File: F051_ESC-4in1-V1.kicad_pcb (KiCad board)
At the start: 4 copper layers, 46 x 55.8 mm, 222 parts, among them J1 Conn_01x02, J11 Conn_01x03, J14 Conn_01x03, J2 Conn_01x10, J3 Conn_01x05, J4 Conn_01x05, J5 Conn_01x05, J6 Conn_01x03, J7 Conn_01x05, J8 Conn_01x03, J9 Conn_01x10, Q1 TPHR8504PL, Q10 TPHR8504PL, Q11 TPHR8504PL, Q12 TPHR8504PL, Q13 TPHR8504PL, Q14 TPHR8504PL, Q15 TPHR8504PL, Q16 TPHR8504PL, Q17 TPHR8504PL, Q18 TPHR8504PL, Q19 TPHR8504PL, Q2 TPHR8504PL, Q20 TPHR8504PL, Q21 TPHR8504PL, Q22 TPHR8504PL, Q23 TPHR8504PL, Q24 TPHR8504PL, Q3 TPHR8504PL, Q4 TPHR8504PL, Q5 TPHR8504PL, Q6 TPHR8504PL, Q7 TPHR8504PL, Q8 TPHR8504PL, Q9 TPHR8504PL, U1 STM32F051K6Ux, U10 FD6288Q, U11 STM32F051K6Ux, U12 FD6288Q, U13 L78L12_SOT89, U14 MP4560_QFN10, U2 FD6288Q, U3 L78L12_SOT89, U4 LP2985-3.3, U5 INA139, U6 FD6288Q, U7 OPA340NA, U8 STM32F051K6Ux, U9 STM32F051K6Ux

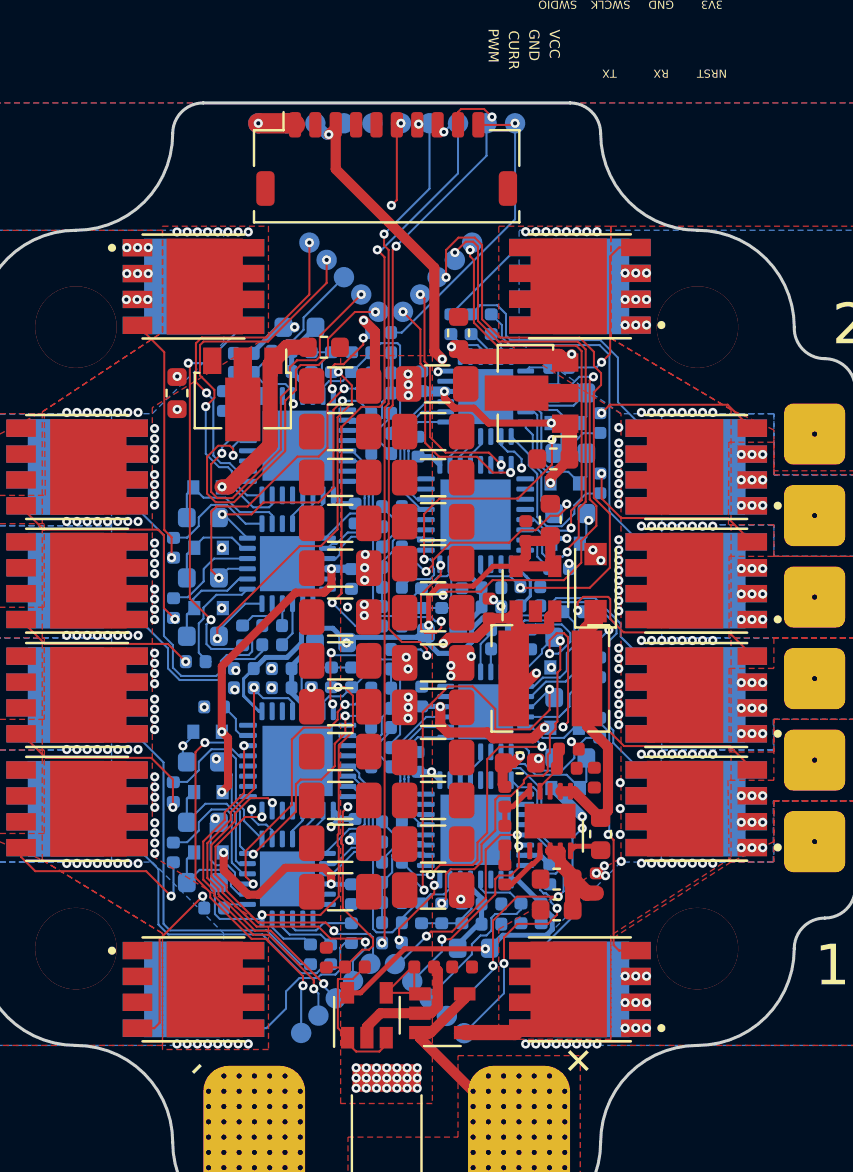
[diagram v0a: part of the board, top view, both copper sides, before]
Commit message: More GND and VCC vias and planes added.  Moved around some sense resistors to expose GND
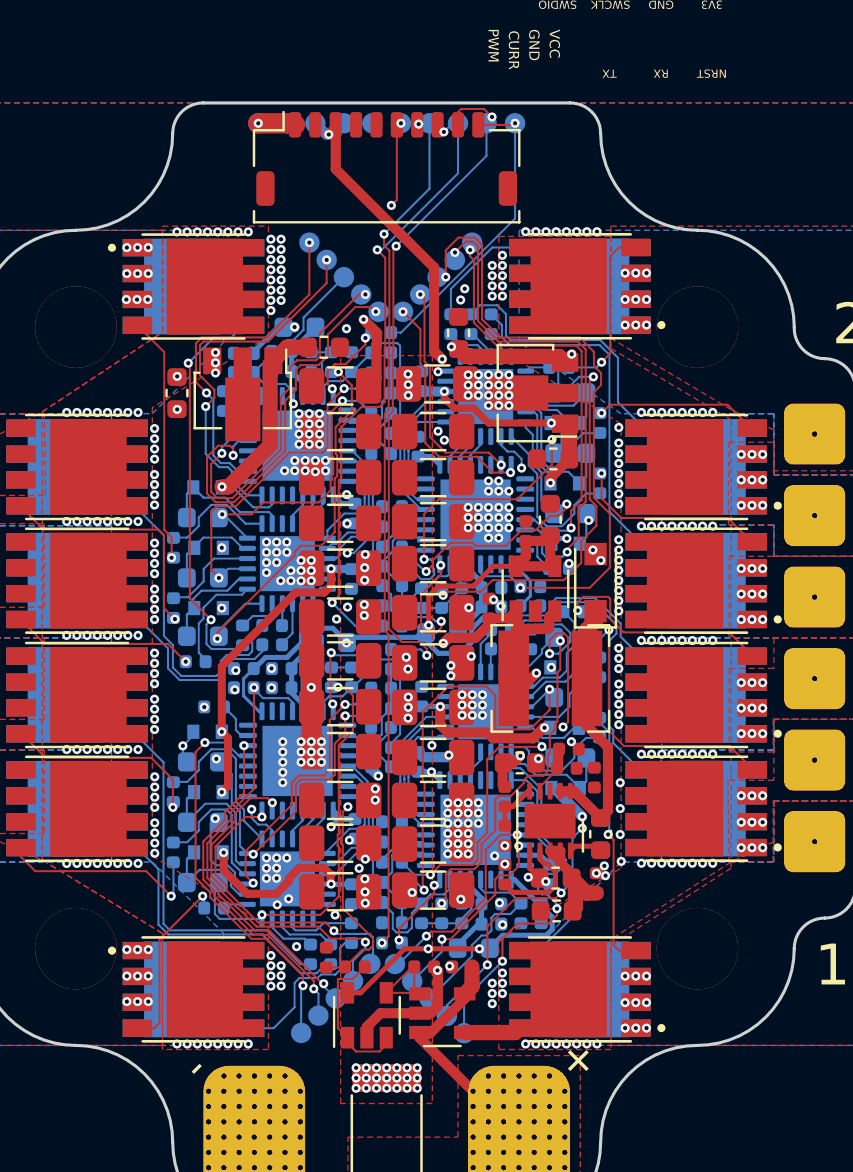
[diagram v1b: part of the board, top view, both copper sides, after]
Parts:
- moved R35 1.90 mm to (140.3, 86.9), turned to 0 degrees
- moved R29 1.04 mm to (140.3, 85.0)
- moved R30 1.02 mm to (140.3, 85.9), turned to 180 degrees
- moved R10 0.99 mm to (140.3, 101.5), turned to 180 degrees
- moved R15 0.99 mm to (140.3, 102.5), turned to 0 degrees
- moved C73 0.07 mm to (148.3, 100.3)
- moved C72 0.05 mm to (148.3, 101.9)
- turned R14 to 0 degrees
- turned R34 to 0 degrees
- turned R36 to 90 degrees
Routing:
- net GND: track 8.15 -> 21.9 mm, vias 141 -> 329
- net +3V3: track 70.6 -> 82.1 mm, vias 7 -> 12
- net Net-(R76-Pad1): track 2.59 -> 4.89 mm
- net VCC: track 7.09 -> 8.55 mm
- net VCC_Shunt: track 21.6 -> 20.2 mm, vias 151 -> 163
- net /MCU 2/SenseC: track 4.67 -> 3.73 mm
- net Net-(Q12-Pad4): track 4.94 -> 5.67 mm
- net /MCU 2/SenseB: track 5.18 -> 5.69 mm
- net /MCU 3/PhaseC: vias 2 -> 11

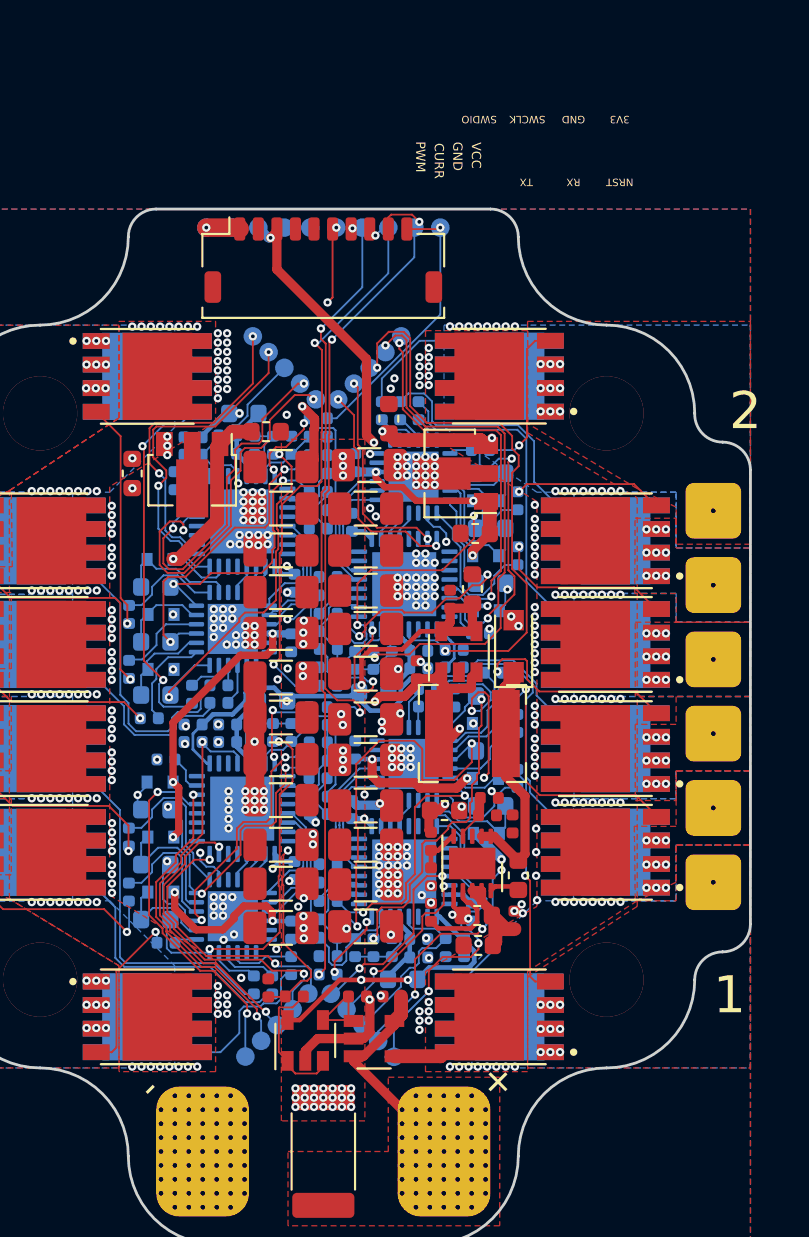
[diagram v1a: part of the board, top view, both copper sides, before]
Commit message: Finished all traces and vias
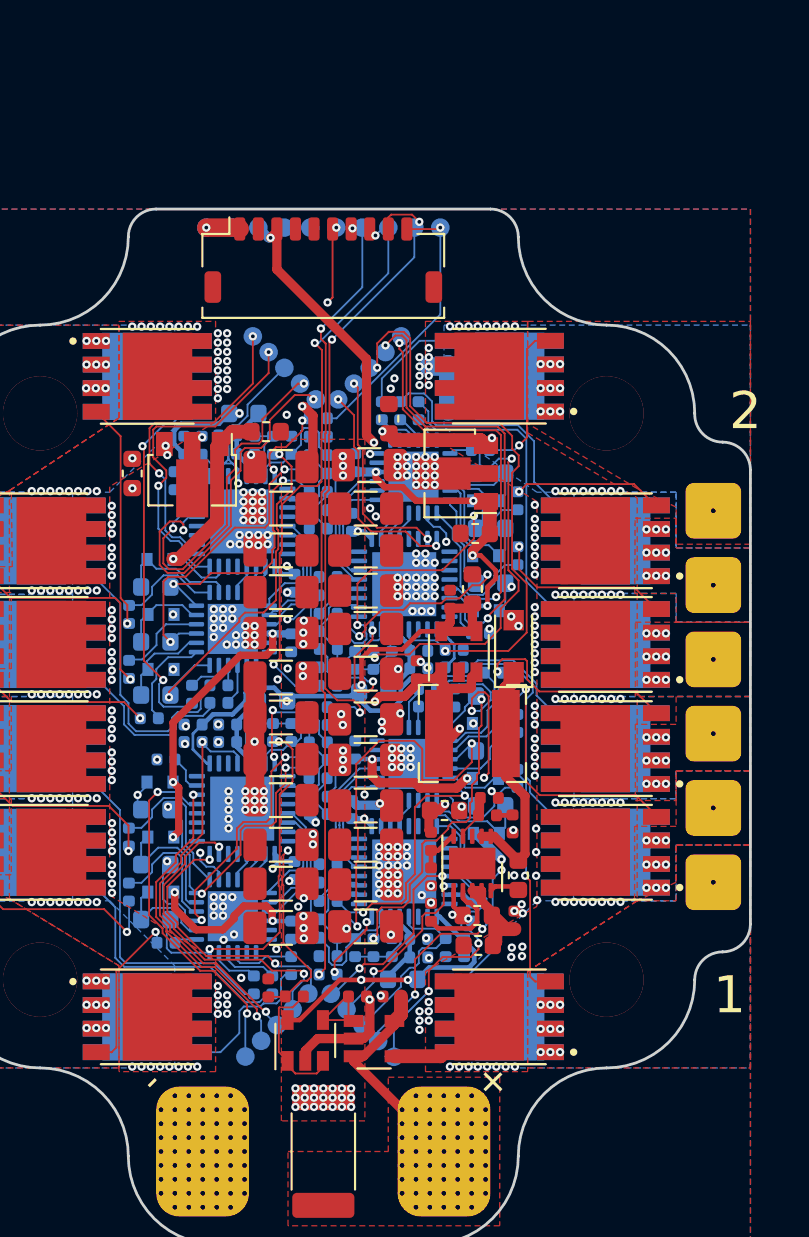
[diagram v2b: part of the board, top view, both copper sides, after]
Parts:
- moved R63 1.98 mm to (139.7, 74.5), turned to 180 degrees
- moved R46 1.93 mm to (139.7, 90.0), turned to 180 degrees
- moved R57 0.99 mm to (139.7, 76.5)
- moved R58 0.99 mm to (139.7, 75.5), turned to 0 degrees
- moved R40 0.94 mm to (139.7, 91.9)
- moved R41 0.94 mm to (139.7, 91.0), turned to 0 degrees
- moved C45 0.69 mm to (133.4, 75.0), turned to 90 degrees
- moved C43 0.64 mm to (132.5, 75.0), turned to 90 degrees
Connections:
- C1 pad 1: +3.3VA -> +3.3VA_1
- C12 pad 1: +12V -> +12V_2
- C2 pad 1: +3.3VA -> +3.3VA_1
- C27 pad 1: +3.3VA -> +3.3VA_2
- C28 pad 1: +3.3VA -> +3.3VA_2
- C32 pad 1: +3.3VA -> +3.3VA_3
- C33 pad 1: +3.3VA -> +3.3VA_3
- C37 pad 1: +12V -> +12V_1
- C41 pad 1: +3.3VA -> +3.3VA_4
- C42 pad 1: +3.3VA -> +3.3VA_4
- C46 pad 1: +12V -> +12V_1
- C5 pad 1: +12V -> +12V_2
- C69 pad 1: +12V -> +12V_1
- C9 pad 1: +12V -> +12V_2
- D1 pad 2: +12V -> +12V_2
- D10 pad 2: +12V -> +12V_1
- D11 pad 2: +12V -> +12V_1
- D12 pad 2: +12V -> +12V_1
- D2 pad 2: +12V -> +12V_2
- D3 pad 2: +12V -> +12V_2
- D4 pad 2: +12V -> +12V_2
- D5 pad 2: +12V -> +12V_2
- D6 pad 2: +12V -> +12V_2
- D7 pad 2: +12V -> +12V_1
- D8 pad 2: +12V -> +12V_1
- D9 pad 2: +12V -> +12V_1
- FB1 pad 1: +3.3VA -> +3.3VA_1
- FB2 pad 1: +3.3VA -> +3.3VA_2
- FB3 pad 1: +3.3VA -> +3.3VA_3
- FB4 pad 1: +3.3VA -> +3.3VA_4
- U1 pad 5: +3.3VA -> +3.3VA_1
- U10 pad 4: +12V -> +12V_1
- U11 pad 5: +3.3VA -> +3.3VA_4
- U12 pad 4: +12V -> +12V_1
- U13 pad 1: +12V -> +12V_1
- U2 pad 4: +12V -> +12V_2
- U3 pad 1: +12V -> +12V_2
- U6 pad 4: +12V -> +12V_2
- U8 pad 5: +3.3VA -> +3.3VA_2
- U9 pad 5: +3.3VA -> +3.3VA_3
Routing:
- net +12V: track 58.2 -> 0.00 mm, vias 16 -> 0
- net +12V_1: track 0.00 -> 33.8 mm, vias 0 -> 8
- net +12V_2: track 0.00 -> 28.0 mm, vias 0 -> 8
- net +3.3VA: track 16.4 -> 0.00 mm
- net GND: track 21.9 -> 26.6 mm, vias 329 -> 334
- net +3.3VA_1: track 0.00 -> 4.17 mm
- net +3.3VA_4: track 0.00 -> 4.08 mm
- net +3.3VA_3: track 0.00 -> 4.08 mm
- net +3.3VA_2: track 0.00 -> 4.02 mm
- net +3V3: track 82.1 -> 84.4 mm, vias 12 -> 13
- net /MCU 4/NRST: track 10.5 -> 11.5 mm
- net Net-(C75-Pad2): track 0.00 -> 0.88 mm
- net VCC_Shunt: vias 163 -> 166
- added copper zone on In2.Cu, net +12V_1
- added copper zone on In2.Cu, net +12V_2
- removed copper zone on In2.Cu, net +12V
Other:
- board text added: "5V"
- board text added: "M1"
- board text added: "M2"
- board text added: "M3"
- board text added: "M4"
- board text removed: "3V3"
- board text removed: "NRST"
- board text removed: "PWM"
- board text removed: "RX"
- board text removed: "SWCLK"
- board text removed: "SWDIO"
- board text removed: "TX"

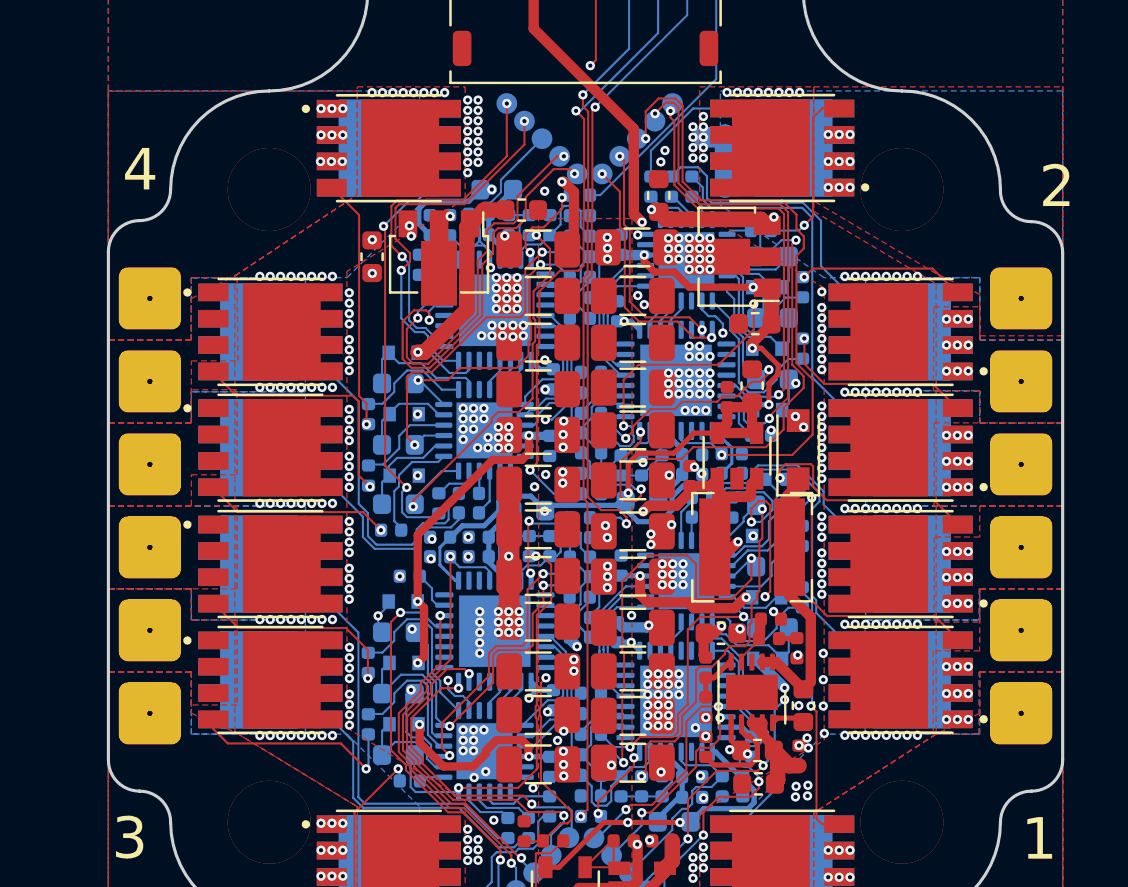
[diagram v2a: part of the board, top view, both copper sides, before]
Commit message: Moved around some traces to create bigger fills
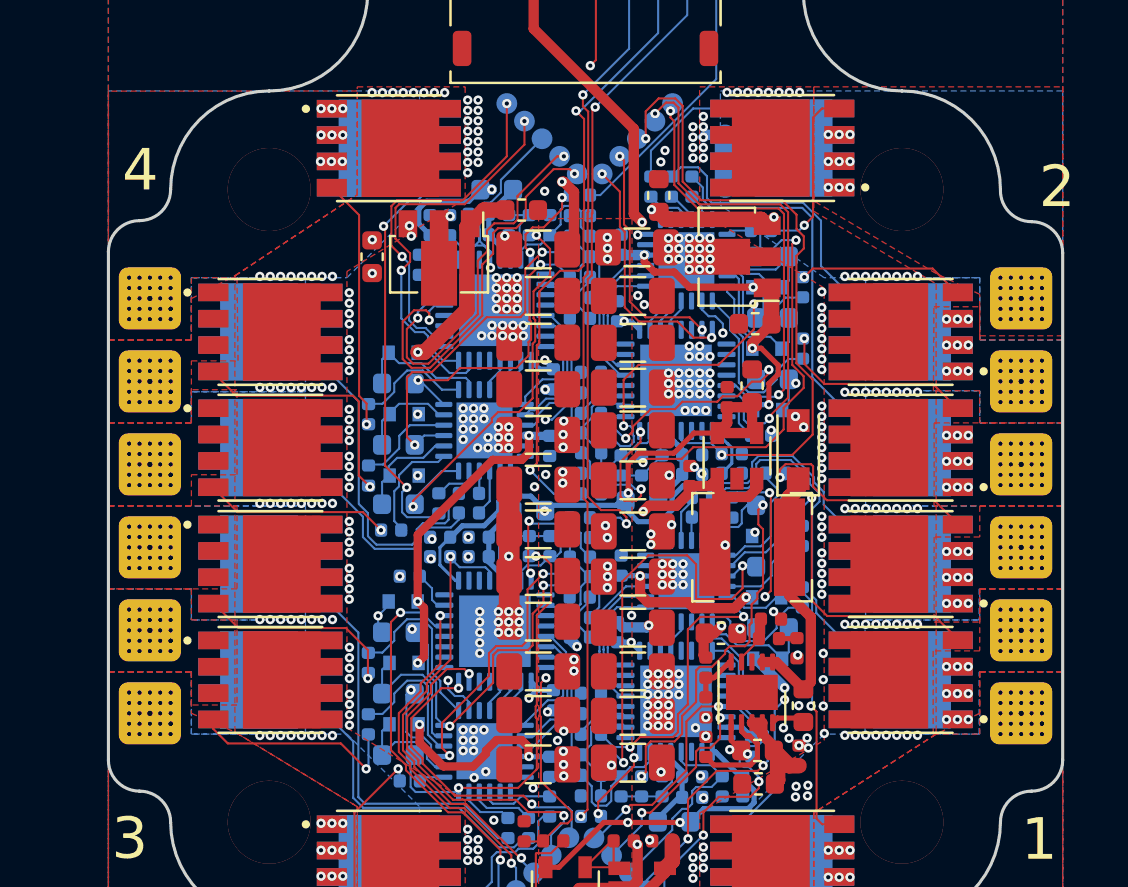
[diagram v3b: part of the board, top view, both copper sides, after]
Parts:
- moved R23 0.30 mm to (149.2, 86.9)
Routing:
- net Net-(Q2-Pad4): track 23.5 -> 20.4 mm
- net /MCU 1/PhaseC: track 33.7 -> 36.3 mm, vias 11 -> 37
- net /MCU 4/PhaseC: track 34.3 -> 35.8 mm, vias 2 -> 28
- net /MCU 3/PhaseB: track 31.4 -> 32.8 mm, vias 3 -> 29
- net /MCU 2/PhaseA: track 30.6 -> 32.0 mm, vias 11 -> 37
- net /MCU 4/PhaseB: track 30.8 -> 32.2 mm, vias 2 -> 28
- net /MCU 4/PhaseA: track 30.8 -> 32.2 mm, vias 11 -> 37
- net /MCU 3/PhaseC: track 36.3 -> 37.7 mm, vias 11 -> 37
- net /MCU 3/PhaseA: track 31.0 -> 32.4 mm, vias 3 -> 29
- net /MCU 2/PhaseB: track 33.6 -> 35.0 mm, vias 11 -> 37
- net /MCU 1/PhaseA: track 30.2 -> 31.6 mm, vias 11 -> 37
- net +5V: track 50.0 -> 48.8 mm
- net /MCU 1/PhaseB: track 36.2 -> 37.2 mm, vias 11 -> 37
- net Net-(Q4-Pad4): track 15.1 -> 15.9 mm
- net Net-(Q6-Pad4): track 8.86 -> 9.62 mm
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
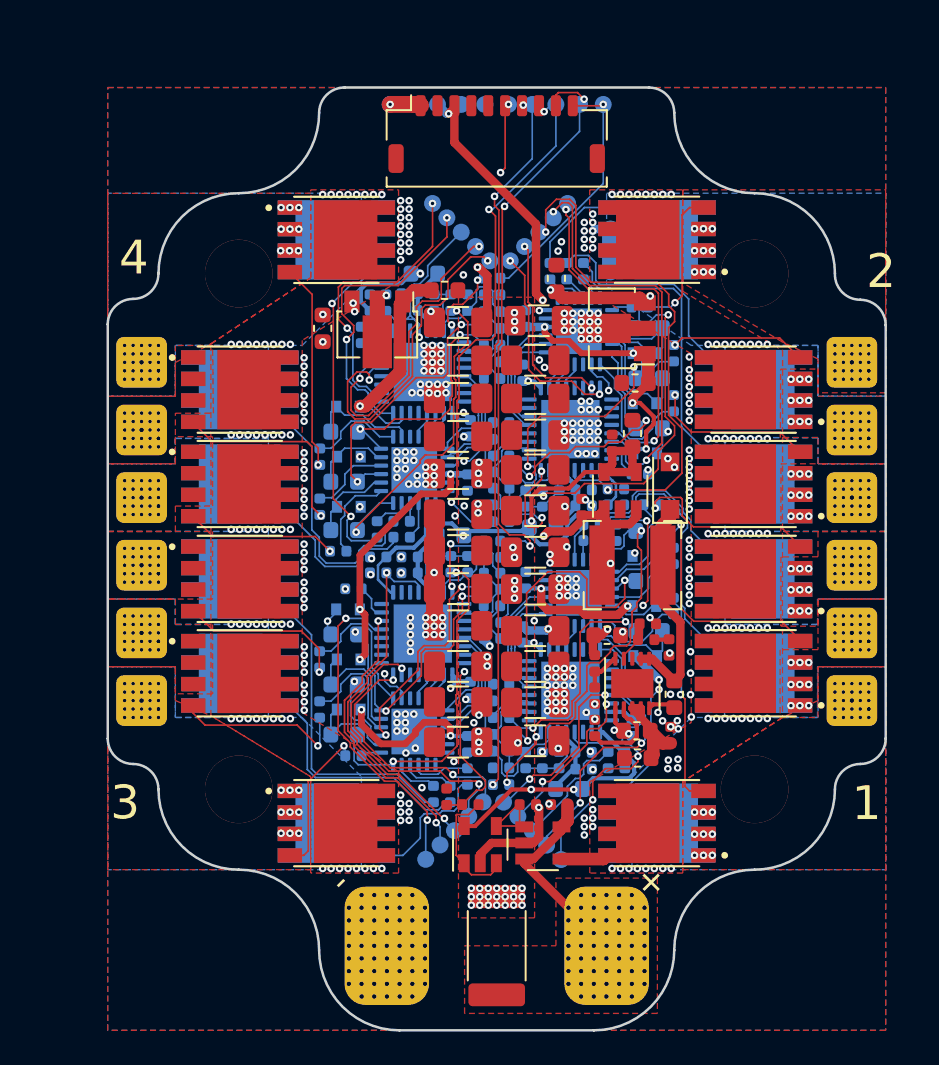
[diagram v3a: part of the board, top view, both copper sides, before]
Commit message: Changed shunt resistor footprint and changed edge cuts to accomodate larger size
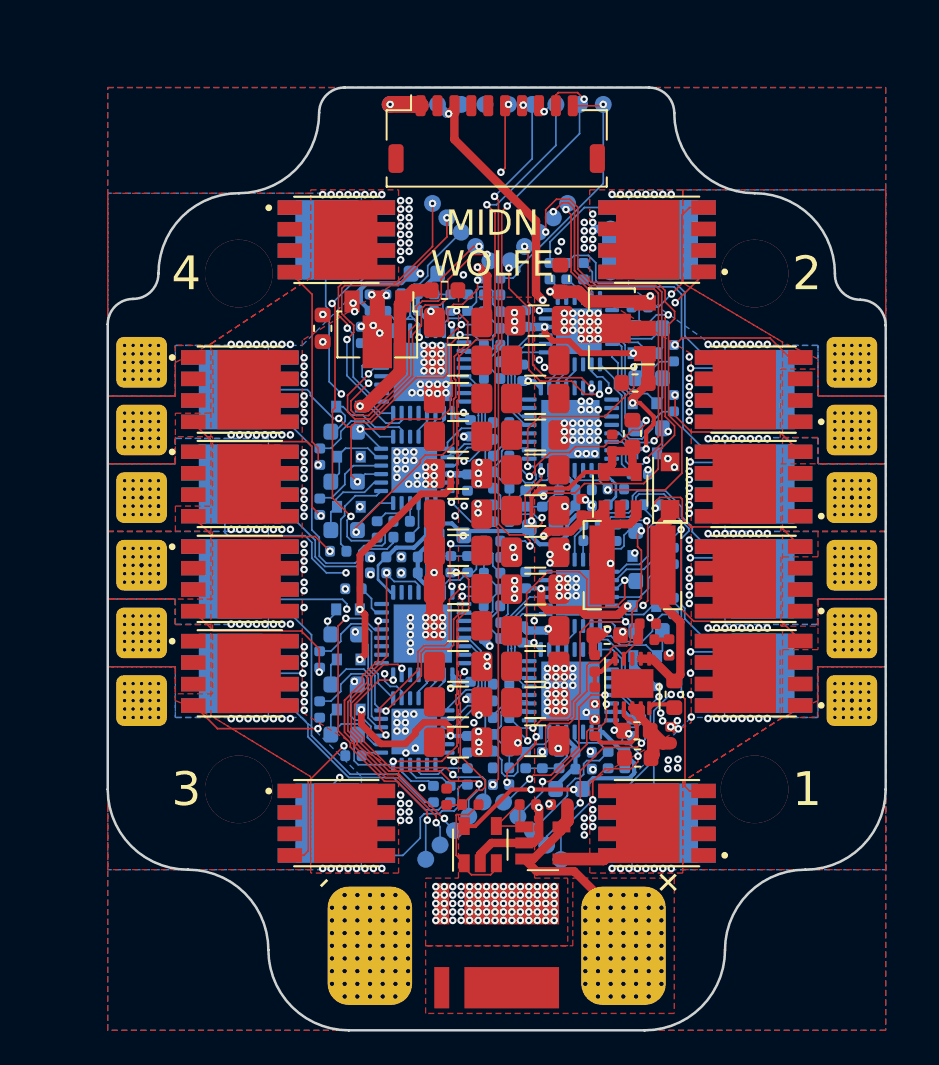
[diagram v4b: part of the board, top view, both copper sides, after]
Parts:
- R1: value 0m30 -> 0m50; footprint Resistor_SMD:R_2512_6332Metric -> Resistor_SMD:R_Shunt_Vishay_WSLP2726
- moved C4 0.24 mm to (143.8, 73.5)
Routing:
- net /MCU 3/PhaseC: track 37.7 -> 27.9 mm, vias 37 -> 28
- net /MCU 2/PhaseC: track 36.6 -> 28.0 mm, vias 37 -> 29
- net /MCU 2/PhaseB: track 35.0 -> 28.6 mm, vias 37 -> 29
- net /MCU 3/PhaseB: track 32.8 -> 26.6 mm
- net /MCU 4/PhaseB: track 32.2 -> 26.2 mm, vias 28 -> 29
- net /MCU 2/PhaseA: track 32.0 -> 26.4 mm, vias 37 -> 29
- net /MCU 1/PhaseC: track 36.3 -> 30.8 mm, vias 37 -> 29
- net /MCU 3/PhaseA: track 32.4 -> 27.0 mm, vias 29 -> 30
- net /MCU 4/PhaseA: track 32.2 -> 27.4 mm, vias 37 -> 29
- net /MCU 1/PhaseB: track 37.2 -> 33.3 mm, vias 37 -> 29
- net /MCU 1/PhaseA: track 31.6 -> 29.6 mm, vias 37 -> 29
- net Net-(Q15-Pad4): track 10.4 -> 8.65 mm
- net /MCU 4/USART1_TX: track 20.1 -> 18.8 mm
- net VCC: track 8.55 -> 9.83 mm
- net Net-(Q16-Pad4): track 14.0 -> 12.9 mm
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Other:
- outline, holes or cut-outs redrawn
